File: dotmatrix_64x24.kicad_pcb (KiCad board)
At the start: 2 copper layers, 180 x 100 mm, 477 parts, among them CON1 BARREL_JACK, P1 CONN_01X09, P2 CONN_01X09, P3 CONN_01X04, P4 CONN_01X03, P5 USB_OTG, P6 CONN_01X03, P7 CONN_01X02, Q1 NJL7302L-F3, Q2 Q_PNP_BEC 2SA1162, Q3 Q_NPN_BCE RN5006, SW1 SW_PUSH_SMALL_H, SW2 SW_PUSH_SMALL_H, SW3 SW_PUSH_SMALL_H, SW4 SW_PUSH_SMALL_H, SW5 SW_PUSH_SMALL_H, SW6 SW_PUSH_SMALL_H, SW7 SW_PUSH_SMALL_H, SW8 SW_PUSH_SMALL_H, U1 WROOM-02, U10 LED1642GW, U11 LED1642GW, U12 AE-BME280, U13 OKL-T/6-W5, U14 NJU7223, U15 DS1307, U16 CH340G, U17 OSRB38C9AA, U2 74HC595-alt-vdd, U3 TD62783, U4 74HC595-alt-vdd, U5 TD62783, U6 LED1642GW, U7 74HC595-alt-vdd, U8 TD62783, U9 LED1642GW, X1 CRYSTAL_SMD, Y1 12MHz

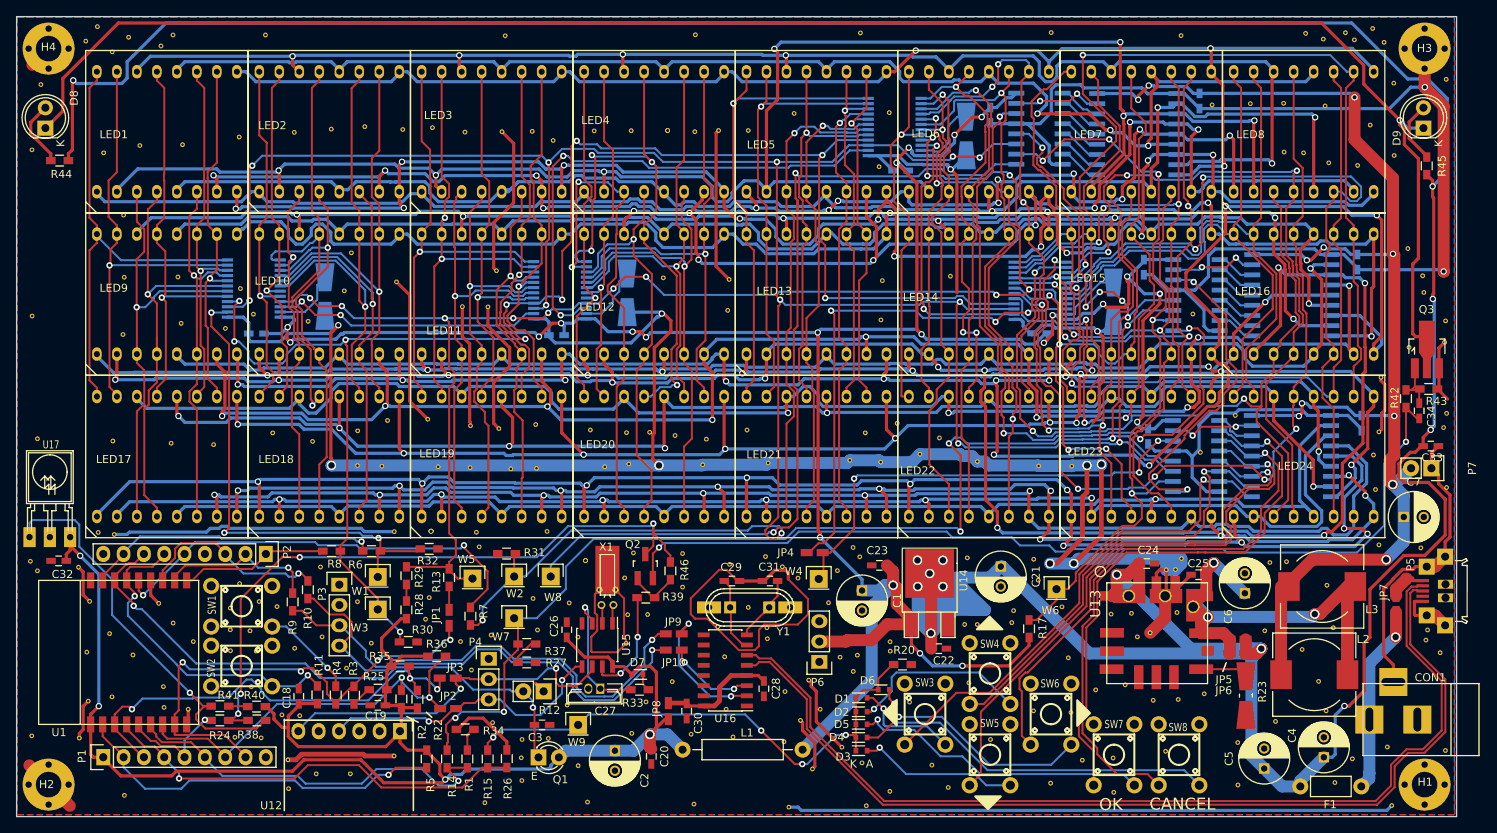
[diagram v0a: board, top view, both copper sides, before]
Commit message: Added BME280 hand-soldering pattern
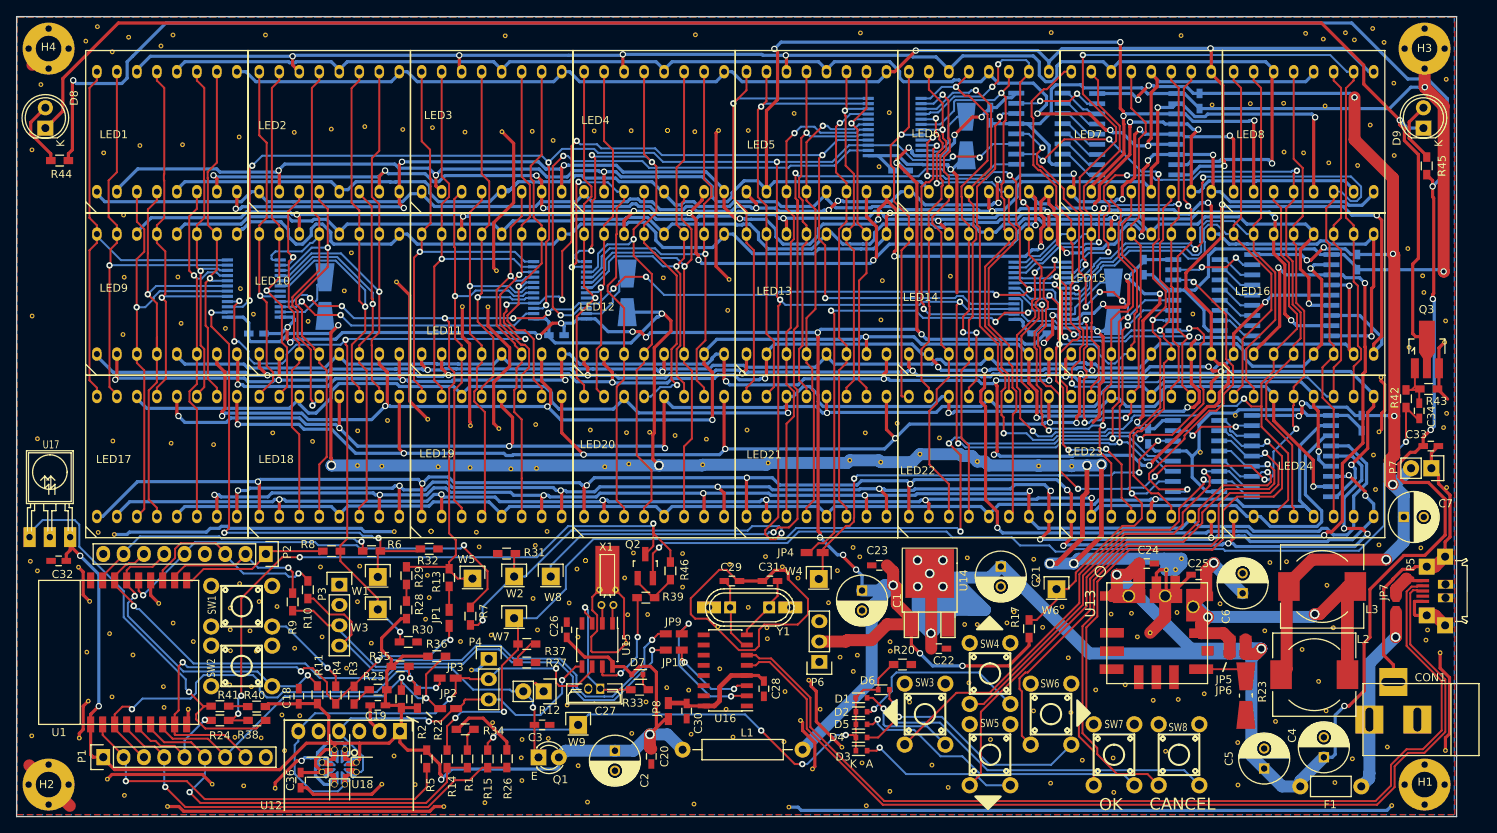
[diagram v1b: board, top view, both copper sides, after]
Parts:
- removed the REF** at (45.9, 104.9)
- removed the REF** at (53.7, 106.7)
- removed the REF** at (49.5, 106.7)
- added C36: 1u, Capacitors_SMD:C_0603_HandSoldering, F.Cu at (47.5, 107.4)
- added REF**: stitch-via-0.6mm, components:stitch-via-0.6mm, F.Cu at (140.3, 88.3)
- added REF**: stitch-via-0.6mm, components:stitch-via-0.6mm, F.Cu at (45.5, 103.8)
- added REF**: stitch-via-0.6mm, components:stitch-via-0.6mm, F.Cu at (61.8, 108.0)
- added REF**: stitch-via-0.6mm, components:stitch-via-0.6mm, F.Cu at (40.4, 108.2)
- added REF**: stitch-via-0.6mm, components:stitch-via-0.6mm, F.Cu at (162.4, 85.4)
- added REF**: stitch-via-0.6mm, components:stitch-via-0.6mm, F.Cu at (23.3, 107.3)
- added REF**: stitch-via-0.6mm, components:stitch-via-0.6mm, F.Cu at (57.7, 108.0)
- added REF**: stitch-via-0.6mm, components:stitch-via-0.6mm, F.Cu at (30.9, 110.7)
- added REF**: stitch-via-0.6mm, components:stitch-via-0.6mm, F.Cu at (65.4, 110.7)
- added REF**: stitch-via-0.6mm, components:stitch-via-0.6mm, F.Cu at (36.4, 108.0)
- added REF**: stitch-via-0.6mm, components:stitch-via-0.6mm, F.Cu at (54.9, 80.7)
- added REF**: stitch-via-0.6mm, components:stitch-via-0.6mm, F.Cu at (38.6, 95.5)
- added REF**: stitch-via-0.6mm, components:stitch-via-0.6mm, F.Cu at (96.0, 96.2)
- added REF**: stitch-via-0.6mm, components:stitch-via-0.6mm, F.Cu at (82.0, 81.1)
- added REF**: stitch-via-0.6mm, components:stitch-via-0.6mm, F.Cu at (76.8, 78.1)
- added REF**: stitch-via-0.6mm, components:stitch-via-0.6mm, F.Cu at (63.3, 81.8)
- added U18: BME280, components:BME280-handsoldering, F.Cu at (52.4, 105.8)
- moved REF** 1.68 mm to (44.3, 108.5)
- moved REF** 1.62 mm to (99.9, 93.5)
- moved REF** 1.03 mm to (93.3, 95.9)
- moved REF** 0.61 mm to (135.8, 87.8)
- moved C6 0.28 mm to (165.3, 84.1)
- moved REF** 0.16 mm to (136.7, 86.4)
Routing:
- net GND: track 901.8 -> 1003.1 mm, vias 12 -> 13
- net /SCL: track 45.2 -> 62.8 mm
- net /SDA: track 36.9 -> 50.4 mm
- net /Sheet57A04605/LEDVDD: track 174.3 -> 163.3 mm
- net /ESPVDD: track 201.4 -> 210.4 mm
- net Net-(P1-Pad6): track 48.8 -> 52.5 mm
- net Net-(P1-Pad2): track 47.5 -> 50.0 mm
- net Net-(P1-Pad4): track 54.6 -> 57.0 mm
- net /Sheet57A04605/SEL4: track 65.7 -> 63.6 mm
- net /Sheet57A04605/SEL3: track 72.1 -> 70.1 mm
- net Net-(U2-Pad14): track 87.9 -> 86.1 mm
- net /Sheet57A04605/SEL2: track 55.1 -> 53.5 mm
- net /Sheet57A04605/SEL1: track 62.8 -> 61.4 mm
- net /Sheet57A04605/c49: track 77.7 -> 76.4 mm
- net /Sheet57A04605/r5: track 176.1 -> 174.9 mm
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
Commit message: Adjusted Via diameter
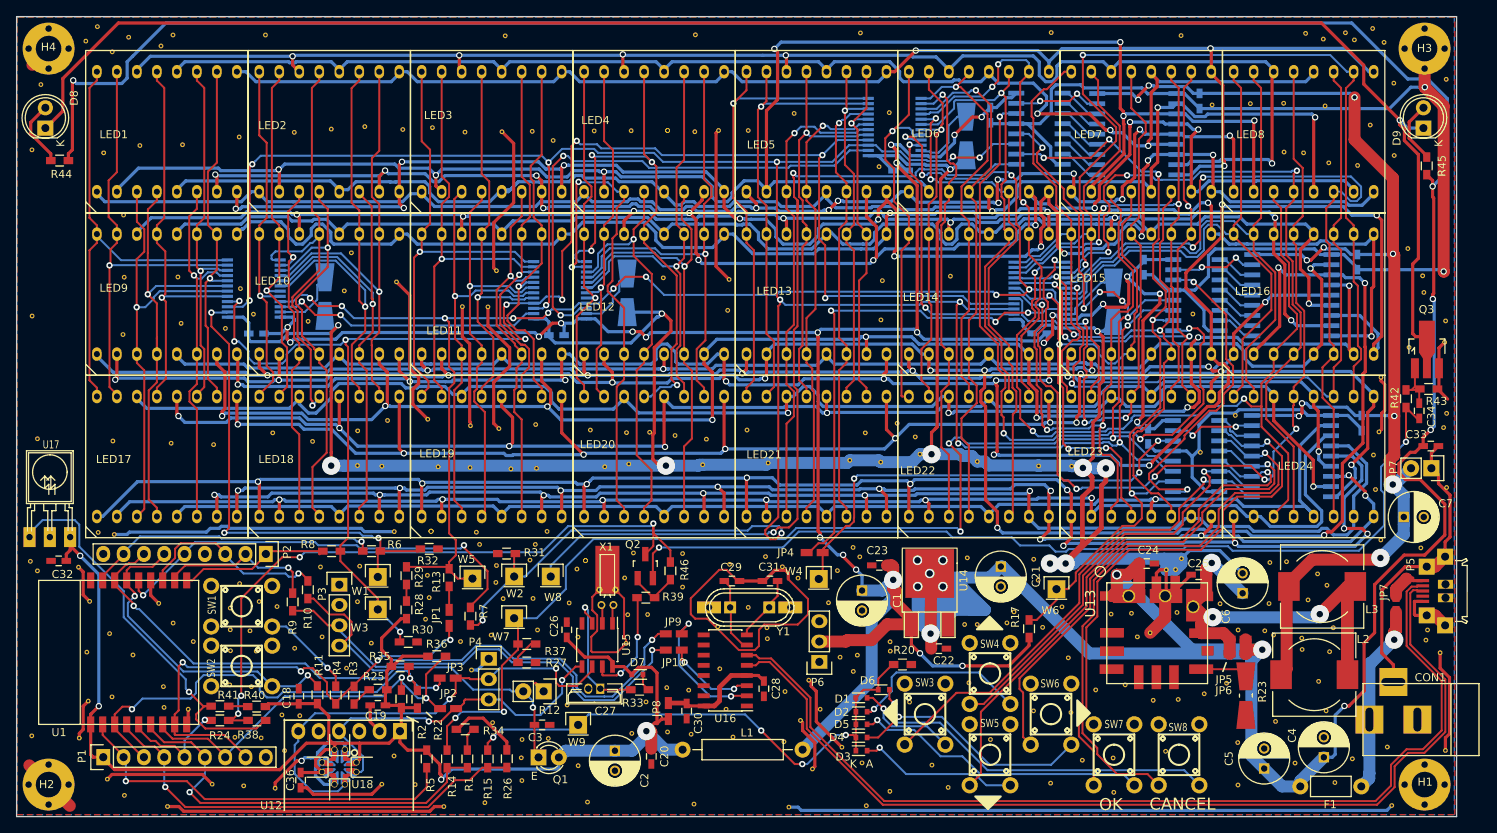
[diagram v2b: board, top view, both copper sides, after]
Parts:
- added REF**: stitch-via-0.6mm, components:stitch-via-0.6mm, F.Cu at (174.6, 81.7)
- added REF**: stitch-via-0.6mm, components:stitch-via-0.6mm, F.Cu at (93.4, 101.4)
- added REF**: stitch-via-0.6mm, components:stitch-via-0.6mm, F.Cu at (72.8, 84.8)
- added REF**: stitch-via-0.6mm, components:stitch-via-0.6mm, F.Cu at (71.9, 82.7)
- added REF**: stitch-via-0.6mm, components:stitch-via-0.6mm, F.Cu at (72.0, 80.6)
- added REF**: stitch-via-0.6mm, components:stitch-via-0.6mm, F.Cu at (76.2, 79.9)
- added REF**: stitch-via-0.6mm, components:stitch-via-0.6mm, F.Cu at (164.7, 88.7)
- added REF**: stitch-via-0.6mm, components:stitch-via-0.6mm, F.Cu at (171.8, 105.3)
- added REF**: stitch-via-0.6mm, components:stitch-via-0.6mm, F.Cu at (163.2, 95.3)
- added REF**: stitch-via-0.6mm, components:stitch-via-0.6mm, F.Cu at (176.1, 91.4)
- added REF**: stitch-via-0.6mm, components:stitch-via-0.6mm, F.Cu at (173.4, 84.9)
- added REF**: stitch-via-0.6mm, components:stitch-via-0.6mm, F.Cu at (168.6, 85.4)
- added REF**: stitch-via-0.6mm, components:stitch-via-0.6mm, F.Cu at (169.1, 89.3)
- added REF**: stitch-via-0.6mm, components:stitch-via-0.6mm, F.Cu at (172.6, 89.7)
- moved REF** 3.03 mm to (124.3, 64.5)
- moved REF** 0.65 mm to (182.5, 77.4)
- moved REF** 0.31 mm to (69.9, 78.0)
- moved REF** 0.13 mm to (76.8, 78.0)
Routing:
- net GND: track 1003.1 -> 1042.5 mm, vias 13 -> 14
- net VCC: track 514.4 -> 510.5 mm
- net /Sheet57A04605/r11: track 244.5 -> 248.0 mm
- net /Sheet57A04605/r12: track 170.8 -> 173.8 mm
- net /LEDLOGICVDD: track 314.2 -> 316.9 mm
- net /Sheet57A04605/COLPWCLK: track 179.5 -> 182.2 mm
- net /Sheet57A04605/c48: track 46.2 -> 48.6 mm
- net /Sheet57A04605/r16: track 170.9 -> 169.0 mm
- net /Sheet57A04605/c42: track 60.5 -> 58.7 mm
- net /Sheet57A04605/c41: track 52.2 -> 50.7 mm, vias 3 -> 1
- net /Sheet57A04605/r23: track 182.1 -> 180.9 mm
- net /Sheet57A04605/SEL5: track 69.1 -> 67.9 mm
- net /Sheet57A04605/c50: track 72.9 -> 74.0 mm
- net Net-(U10-Pad22): track 35.1 -> 34.1 mm
- net /Sheet57A04605/SEL6: track 76.0 -> 75.1 mm
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
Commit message: Various fixes
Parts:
- removed P7: CONN_01X02, Pin_Headers:Pin_Header_Straight_1x02
- added JP11: Jumper_NC_Small, components:SolderJumper, F.Cu at (184.5, 76.0)
- added JP12: Jumper_NC_Small, components:SolderJumper, F.Cu at (186.2, 76.0)
- added REF**: stitch-via-0.6mm, components:stitch-via-0.6mm, F.Cu at (64.3, 89.6)
- added REF**: stitch-via-0.6mm, components:stitch-via-0.6mm, F.Cu at (152.5, 88.2)
- added REF**: stitch-via-0.6mm, components:stitch-via-0.6mm, F.Cu at (182.8, 107.8)
- added REF**: stitch-via-0.6mm, components:stitch-via-0.6mm, F.Cu at (174.9, 108.7)
- added REF**: stitch-via-0.6mm, components:stitch-via-0.6mm, F.Cu at (141.0, 104.3)
- added REF**: stitch-via-0.6mm, components:stitch-via-0.6mm, F.Cu at (157.0, 107.3)
- added REF**: stitch-via-0.6mm, components:stitch-via-0.6mm, F.Cu at (144.7, 109.0)
- added REF**: stitch-via-0.6mm, components:stitch-via-0.6mm, F.Cu at (138.3, 109.2)
- added REF**: stitch-via-0.6mm, components:stitch-via-0.6mm, F.Cu at (133.7, 109.0)
- added REF**: stitch-via-0.6mm, components:stitch-via-0.6mm, F.Cu at (125.7, 95.3)
- added REF**: stitch-via-0.6mm, components:stitch-via-0.6mm, F.Cu at (93.4, 92.7)
- added REF**: stitch-via-0.6mm, components:stitch-via-0.6mm, F.Cu at (57.5, 88.6)
- added REF**: stitch-via-0.6mm, components:stitch-via-0.6mm, F.Cu at (93.3, 87.7)
- added REF**: stitch-via-0.6mm, components:stitch-via-0.6mm, F.Cu at (87.8, 88.1)
- added REF**: stitch-via-0.6mm, components:stitch-via-0.6mm, F.Cu at (80.9, 91.4)
- added REF**: stitch-via-0.6mm, components:stitch-via-0.6mm, F.Cu at (28.5, 92.2)
- added REF**: stitch-via-0.6mm, components:stitch-via-0.6mm, F.Cu at (23.5, 84.5)
- added REF**: stitch-via-0.6mm, components:stitch-via-0.6mm, F.Cu at (167.9, 100.7)
- added REF**: stitch-via-0.6mm, components:stitch-via-0.6mm, F.Cu at (167.9, 99.3)
- added REF**: stitch-via-0.6mm, components:stitch-via-0.6mm, F.Cu at (180.4, 91.1)
- added REF**: stitch-via-0.6mm, components:stitch-via-0.6mm, F.Cu at (178.3, 99.8)
- added REF**: stitch-via-0.6mm, components:stitch-via-0.6mm, F.Cu at (187.5, 94.5)
- added REF**: stitch-via-0.6mm, components:stitch-via-0.6mm, F.Cu at (188.1, 27.8)
- added REF**: stitch-via-0.6mm, components:stitch-via-0.6mm, F.Cu at (188.9, 96.7)
- added REF**: stitch-via-0.6mm, components:stitch-via-0.6mm, F.Cu at (185.2, 92.1)
- added REF**: stitch-via-0.6mm, components:stitch-via-0.6mm, F.Cu at (181.8, 86.9)
- added REF**: stitch-via-0.6mm, components:stitch-via-0.6mm, F.Cu at (180.8, 87.8)
- added REF**: stitch-via-0.6mm, components:stitch-via-0.6mm, F.Cu at (180.2, 86.6)
- added REF**: stitch-via-0.6mm, components:stitch-via-0.6mm, F.Cu at (180.1, 89.8)
- added REF**: stitch-via-0.6mm, components:stitch-via-0.6mm, F.Cu at (175.1, 96.5)
- added REF**: stitch-via-0.6mm, components:stitch-via-0.6mm, F.Cu at (174.9, 94.2)
- added REF**: stitch-via-0.6mm, components:stitch-via-0.6mm, F.Cu at (174.2, 92.6)
- added REF**: stitch-via-0.6mm, components:stitch-via-0.6mm, F.Cu at (163.4, 101.0)
- added REF**: stitch-via-0.6mm, components:stitch-via-0.6mm, F.Cu at (185.8, 23.7)
- added REF**: stitch-via-0.6mm, components:stitch-via-0.6mm, F.Cu at (167.8, 97.6)
- added REF**: stitch-via-0.6mm, components:stitch-via-0.6mm, F.Cu at (162.8, 97.9)
- added REF**: stitch-via-0.6mm, components:stitch-via-0.6mm, F.Cu at (171.8, 99.7)
- added REF**: stitch-via-0.6mm, components:stitch-via-0.6mm, F.Cu at (171.7, 101.1)
- added REF**: stitch-via-0.6mm, components:stitch-via-0.6mm, F.Cu at (171.7, 97.6)
- added REF**: stitch-via-0.6mm, components:stitch-via-0.6mm, F.Cu at (68.8, 97.9)
- added REF**: stitch-via-0.6mm, components:stitch-via-0.6mm, F.Cu at (72.1, 104.7)
- added REF**: stitch-via-0.6mm, components:stitch-via-0.6mm, F.Cu at (69.6, 104.8)
- added REF**: stitch-via-0.6mm, components:stitch-via-0.6mm, F.Cu at (67.1, 104.8)
- added REF**: stitch-via-0.6mm, components:stitch-via-0.6mm, F.Cu at (71.5, 100.3)
- added REF**: stitch-via-0.6mm, components:stitch-via-0.6mm, F.Cu at (187.7, 49.1)
- added REF**: stitch-via-0.6mm, components:stitch-via-0.6mm, F.Cu at (73.8, 94.6)
- added REF**: stitch-via-0.6mm, components:stitch-via-0.6mm, F.Cu at (74.5, 99.1)
- added REF**: stitch-via-0.6mm, components:stitch-via-0.6mm, F.Cu at (22.4, 72.3)
- added REF**: stitch-via-0.6mm, components:stitch-via-0.6mm, F.Cu at (13.4, 73.0)
- added REF**: stitch-via-0.6mm, components:stitch-via-0.6mm, F.Cu at (123.3, 98.5)
- added REF**: stitch-via-0.6mm, components:stitch-via-0.6mm, F.Cu at (121.2, 102.1)
- added REF**: stitch-via-0.6mm, components:stitch-via-0.6mm, F.Cu at (129.1, 99.0)
- added REF**: stitch-via-0.6mm, components:stitch-via-0.6mm, F.Cu at (134.3, 99.3)
- added REF**: stitch-via-0.6mm, components:stitch-via-0.6mm, F.Cu at (134.0, 91.8)
- added REF**: stitch-via-0.6mm, components:stitch-via-0.6mm, F.Cu at (134.3, 94.2)
- added REF**: stitch-via-0.6mm, components:stitch-via-0.6mm, F.Cu at (181.6, 81.7)
- added REF**: stitch-via-0.6mm, components:stitch-via-0.6mm, F.Cu at (115.5, 88.4)
- added REF**: stitch-via-0.6mm, components:stitch-via-0.6mm, F.Cu at (125.2, 93.1)
- added REF**: stitch-via-0.6mm, components:stitch-via-0.6mm, F.Cu at (128.2, 92.2)
- added REF**: stitch-via-0.6mm, components:stitch-via-0.6mm, F.Cu at (182.4, 68.7)
- added REF**: stitch-via-0.6mm, components:stitch-via-0.6mm, F.Cu at (186.6, 65.1)
- added REF**: stitch-via-0.6mm, components:stitch-via-0.6mm, F.Cu at (186.6, 64.0)
- moved REF** 9.08 mm to (161.2, 104.1)
- moved REF** 6.22 mm to (19.6, 104.4)
- moved C7 5.64 mm to (185.3, 68.9)
- moved REF** 5.53 mm to (172.3, 93.8)
- moved REF** 3.46 mm to (188.5, 73.5)
- moved REF** 2.14 mm to (122.8, 91.5)
- moved REF** 1.52 mm to (138.2, 68.2)
- moved C33 1.30 mm to (188.9, 64.4)
- moved REF** 1.08 mm to (176.8, 87.3)
- moved REF** 1.07 mm to (14.7, 80.2)
- moved C2 1.00 mm to (85.8, 104.0)
- moved REF** 0.96 mm to (171.9, 91.6)
- moved REF** 0.92 mm to (182.8, 63.1)
- moved REF** 0.85 mm to (22.0, 29.2)
- moved REF** 0.65 mm to (20.4, 102.5)
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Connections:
- L2 pad 2: /Sheet57A04605/LEDVDD -> Net-(JP11-Pad1)
- L3 pad 2: /Sheet57A04605/LEDVDD -> Net-(JP11-Pad1)
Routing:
- net VCC: track 510.5 -> 570.9 mm, vias 13 -> 14
- net /Sheet57A04605/LEDVDD: track 162.7 -> 131.0 mm, vias 11 -> 10
- net Net-(JP11-Pad1): track 0.00 -> 30.0 mm
- net GND: track 1042.5 -> 1024.9 mm
- net /Sheet57A04605/r3: track 206.2 -> 202.6 mm
- net /Sheet57A04605/r12: track 173.8 -> 170.6 mm
- net /Sheet57A04605/r21: track 213.6 -> 211.5 mm
- net /Sheet57A04605/r22: track 178.2 -> 176.1 mm
- net /Sheet57A04605/r16: track 169.0 -> 167.4 mm
- net /SDA: track 50.4 -> 51.8 mm
- net /Sheet57A04605/r18: track 178.0 -> 179.3 mm
- net /Sheet57A04605/COLPWCLK: track 182.2 -> 181.0 mm
- net /Sheet57A04605/r8: track 181.6 -> 180.6 mm
- net /Sheet57A04605/HC595LATCH: track 186.6 -> 185.7 mm
- net /Sheet57A04605/c50: track 74.0 -> 73.2 mm
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
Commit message: Various fixes
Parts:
- removed the REF** at (64.0, 25.9)
- removed the REF** at (53.8, 41.5)
- added REF**: stitch-via-0.6mm, components:stitch-via-0.6mm, F.Cu at (57.3, 49.2)
- added REF**: stitch-via-0.6mm, components:stitch-via-0.6mm, F.Cu at (128.6, 51.0)
- added REF**: stitch-via-0.6mm, components:stitch-via-0.6mm, F.Cu at (129.9, 43.0)
- added REF**: stitch-via-0.6mm, components:stitch-via-0.6mm, F.Cu at (119.6, 43.3)
- added REF**: stitch-via-0.6mm, components:stitch-via-0.6mm, F.Cu at (118.6, 49.9)
- added REF**: stitch-via-0.6mm, components:stitch-via-0.6mm, F.Cu at (93.4, 48.1)
- added REF**: stitch-via-0.6mm, components:stitch-via-0.6mm, F.Cu at (102.8, 48.0)
- added REF**: stitch-via-0.6mm, components:stitch-via-0.6mm, F.Cu at (102.5, 43.5)
- added REF**: stitch-via-0.6mm, components:stitch-via-0.6mm, F.Cu at (81.5, 21.6)
- added REF**: stitch-via-0.6mm, components:stitch-via-0.6mm, F.Cu at (74.2, 21.4)
- added REF**: stitch-via-0.6mm, components:stitch-via-0.6mm, F.Cu at (66.3, 21.4)
- added REF**: stitch-via-0.6mm, components:stitch-via-0.6mm, F.Cu at (52.8, 43.7)
- added REF**: stitch-via-0.6mm, components:stitch-via-0.6mm, F.Cu at (62.2, 21.8)
- added REF**: stitch-via-0.6mm, components:stitch-via-0.6mm, F.Cu at (56.2, 27.7)
- added REF**: stitch-via-0.6mm, components:stitch-via-0.6mm, F.Cu at (52.7, 21.5)
- added REF**: stitch-via-0.6mm, components:stitch-via-0.6mm, F.Cu at (42.0, 21.9)
- added REF**: stitch-via-0.6mm, components:stitch-via-0.6mm, F.Cu at (37.1, 29.2)
- added REF**: stitch-via-0.6mm, components:stitch-via-0.6mm, F.Cu at (34.3, 29.1)
- added REF**: stitch-via-0.6mm, components:stitch-via-0.6mm, F.Cu at (29.2, 22.7)
- added REF**: stitch-via-0.6mm, components:stitch-via-0.6mm, F.Cu at (21.4, 30.1)
- added REF**: stitch-via-0.6mm, components:stitch-via-0.6mm, F.Cu at (160.3, 44.6)
- added REF**: stitch-via-0.6mm, components:stitch-via-0.6mm, F.Cu at (140.6, 26.0)
- added REF**: stitch-via-0.6mm, components:stitch-via-0.6mm, F.Cu at (32.2, 95.7)
- added REF**: stitch-via-0.6mm, components:stitch-via-0.6mm, F.Cu at (147.5, 20.2)
- added REF**: stitch-via-0.6mm, components:stitch-via-0.6mm, F.Cu at (59.3, 86.1)
- added REF**: stitch-via-0.6mm, components:stitch-via-0.6mm, F.Cu at (114.6, 107.1)
- added REF**: stitch-via-0.6mm, components:stitch-via-0.6mm, F.Cu at (102.1, 106.4)
- added REF**: stitch-via-0.6mm, components:stitch-via-0.6mm, F.Cu at (17.2, 57.3)
- added REF**: stitch-via-0.6mm, components:stitch-via-0.6mm, F.Cu at (18.8, 46.1)
- added REF**: stitch-via-0.6mm, components:stitch-via-0.6mm, F.Cu at (102.3, 67.5)
- moved REF** 7.35 mm to (45.0, 21.8)
- moved REF** 6.23 mm to (21.2, 23.0)
- moved REF** 5.24 mm to (31.7, 22.9)
- moved REF** 4.06 mm to (55.1, 21.7)
- moved REF** 3.29 mm to (24.8, 30.1)
- moved REF** 2.27 mm to (50.0, 27.9)
- moved REF** 2.25 mm to (58.7, 27.7)
- moved REF** 2.18 mm to (71.4, 28.1)
- moved REF** 1.98 mm to (99.4, 50.0)
- moved REF** 1.92 mm to (47.7, 28.1)
- moved REF** 1.81 mm to (99.4, 45.5)
- moved REF** 1.68 mm to (68.6, 28.0)
- moved REF** 0.56 mm to (29.9, 98.3)
- moved REF** 0.46 mm to (29.9, 95.8)
- moved REF** 0.46 mm to (54.4, 80.7)
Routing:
- net /Sheet57A04605/c14: track 58.3 -> 53.7 mm
- net GND: track 1024.9 -> 1029.2 mm
- net /Sheet57A04605/c13: track 58.8 -> 55.4 mm
- net Net-(P2-Pad3): track 24.0 -> 22.0 mm
- net /Sheet57A04605/c12: track 57.7 -> 56.1 mm
- net /Sheet57A04605/COLLATCH: track 202.4 -> 203.4 mm
- net /ESPVDD: track 211.0 -> 210.1 mm
- net /Sheet57A04605/r5: track 175.4 -> 174.8 mm
- net /Sheet57A04605/COLSER: track 60.8 -> 60.2 mm
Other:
- board text added: "1"
